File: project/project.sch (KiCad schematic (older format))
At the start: 7 parts

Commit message: fix lib
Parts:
- U?: symbol RockPi:RockPi-S -> project-rescue:RockPi-S-RockPi
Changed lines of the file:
@@
 EESchema Schematic File Version 4
+LIBS:project-cache
 EELAYER 26 0
 EELAYER END
@@
 $EndComp
 $Comp
-L RockPi:RockPi-S U?
+L project-rescue:RockPi-S-RockPi U?
 U 1 1 5FF9F2DF
 P 7750 3550

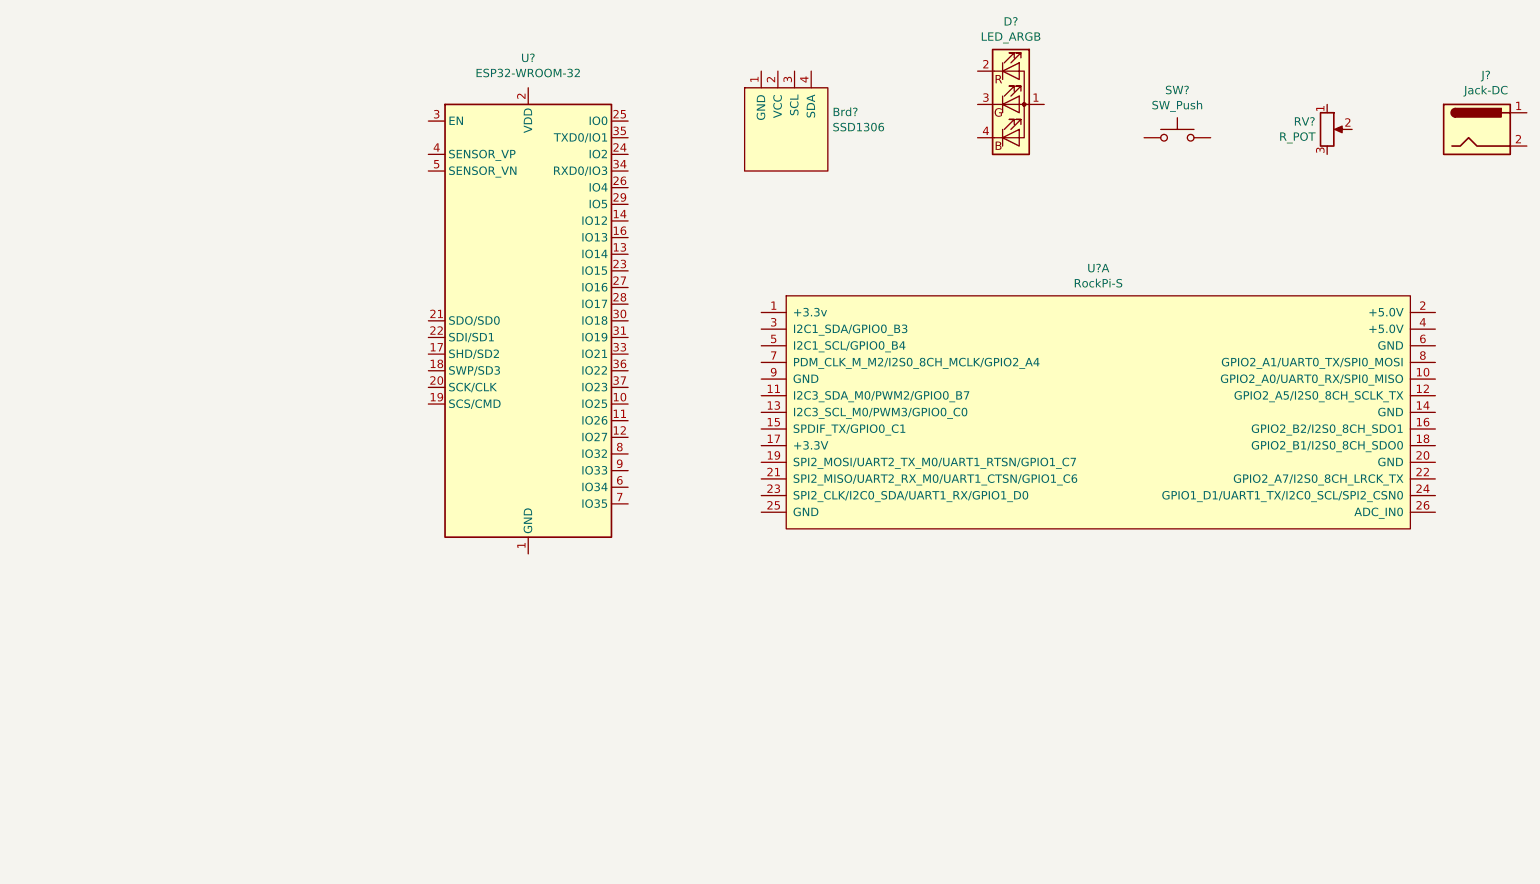
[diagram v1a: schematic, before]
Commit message: add connections, 5V and GND bus
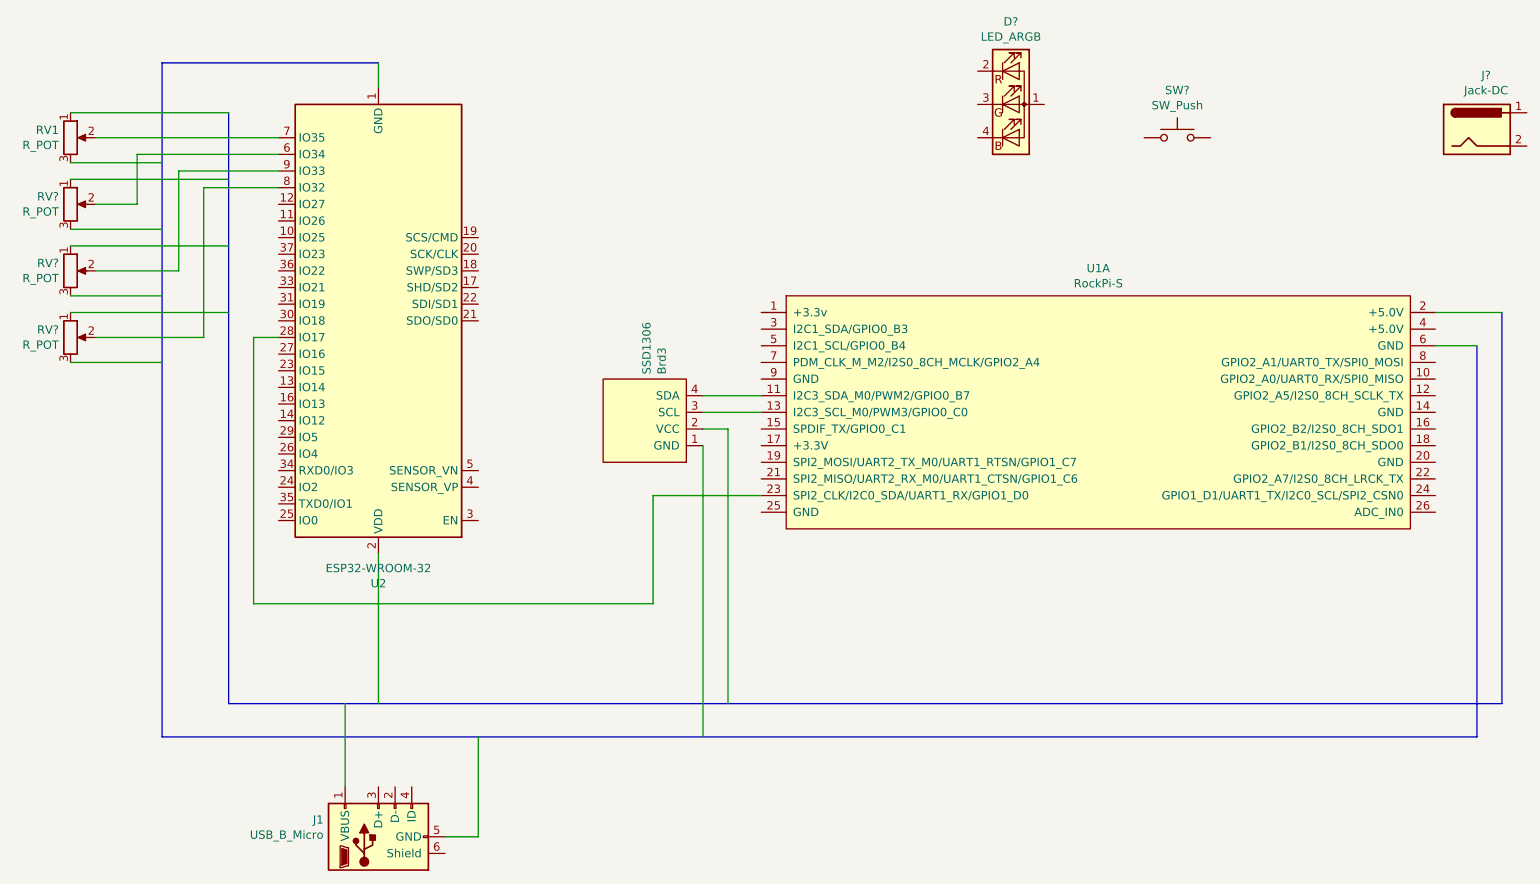
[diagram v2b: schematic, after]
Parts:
- added J1: USB_B_Micro, symbol Connector:USB_B_Micro
- added RV? (x3): R_POT, symbol Device:R_POT
- gave numbers to parts that had none: 4
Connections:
- wire segments 0 -> 35
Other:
- moved on the sheet: Brd3, RV1, U2
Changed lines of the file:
@@
 $EndDescr
 $Comp
-L RF_Module:ESP32-WROOM-32 U?
+L RF_Module:ESP32-WROOM-32 U2
 U 1 1 5FF9F0B8
-P 4200 3000
-F 0 "U?" H 4200 4578 50  0000 C CNN
-F 1 "ESP32-WROOM-32" H 4200 4487 50  0000 C CNN
-F 2 "RF_Module:ESP32-WROOM-32" H 4200 1500 50  0001 C CNN
-F 3 "https://www.espressif.com/sites/default/files/documentation/esp32-wroom-32_datasheet_en.pdf" H 3900 3050 50  0001 C CNN
-	1    4200 3000
-	1    0    0    -1
-$EndComp
-$Comp
-L project-rescue:RockPi-S-RockPi U?
+P 3300 3000
+F 0 "U2" H 3300 4578 50  0000 C CNN
+F 1 "ESP32-WROOM-32" H 3300 4487 50  0000 C CNN
+F 2 "RF_Module:ESP32-WROOM-32" H 3300 1500 50  0001 C CNN
+F 3 "https://www.espressif.com/sites/default/files/documentation/esp32-wroom-32_datasheet_en.pdf" H 3000 3050 50  0001 C CNN
+	1    3300 3000
+	-1   0    0    1
+$EndComp
+$Comp
+L project-rescue:RockPi-S-RockPi U1
 U 1 1 5FF9F2DF
 P 7750 3550
-F 0 "U?" H 7625 4415 50  0000 C CNN
+F 0 "U1" H 7625 4415 50  0000 C CNN
 F 1 "RockPi-S" H 7625 4324 50  0000 C CNN
 F 2 "" H 9600 3600 50  0001 C CNN
@@
 $EndComp
 $Comp
-L SSD1306-128x64_OLED:SSD1306 Brd?
+L SSD1306-128x64_OLED:SSD1306 Brd3
 U 1 1 5FF9F3AC
-P 5750 1850
-F 0 "Brd?" H 6028 1953 50  0000 L CNN
-F 1 "SSD1306" H 6028 1862 50  0000 L CNN
-F 2 "" H 5750 2100 50  0001 C CNN
-F 3 "" H 5750 2100 50  0001 C CNN
-	1    5750 1850
-	1    0    0    -1
+P 4900 3600
+F 0 "Brd3" H 5178 3703 50  0000 L CNN
+F 1 "SSD1306" H 5178 3612 50  0000 L CNN
+F 2 "" H 4900 3850 50  0001 C CNN
+F 3 "" H 4900 3850 50  0001 C CNN
+	1    4900 3600
+	0    1    -1   0
 $EndComp
 $Comp
@@
 $EndComp
 $Comp
-L Device:R_POT RV?
+L Device:R_POT RV1
 U 1 1 5FF9F680
-P 9000 1850
-F 0 "RV?" H 8930 1896 50  0000 R CNN
-F 1 "R_POT" H 8930 1805 50  0000 R CNN
-F 2 "" H 9000 1850 50  0001 C CNN
-F 3 "~" H 9000 1850 50  0001 C CNN
-	1    9000 1850
+P 1450 1900
+F 0 "RV1" H 1380 1946 50  0000 R CNN
+F 1 "R_POT" H 1380 1855 50  0000 R CNN
+F 2 "" H 1450 1900 50  0001 C CNN
+F 3 "~" H 1450 1900 50  0001 C CNN
+	1    1450 1900
 	1    0    0    -1
 $EndComp
@@
 	1    0    0    -1
 $EndComp
+Wire Wire Line
+	5250 3450 5600 3450
+Wire Wire Line
+	5250 3550 5600 3550
+$Comp
+L Connector:USB_B_Micro J1
+U 1 1 5FFA4D52
+P 3300 6100
+F 0 "J1" V 3402 6430 50  0000 L CNN
+F 1 "USB_B_Micro" V 3311 6430 50  0000 L CNN
+F 2 "" H 3450 6050 50  0001 C CNN
+F 3 "~" H 3450 6050 50  0001 C CNN
+	1    3300 6100
+	0    -1   -1   0
+$EndComp
+Wire Wire Line
+	3100 5800 3100 5300
+Wire Wire Line
+	5250 3650 5400 3650
+Wire Wire Line
+	5400 3650 5400 5300
+Wire Wire Line
+	3300 4400 3300 5300
+Wire Bus Line
+	10050 5300 10050 2950
+Wire Wire Line
+	9650 2950 10050 2950
+Wire Bus Line
+	9900 5500 9900 3150
+Wire Wire Line
+	9650 3150 9900 3150
+Wire Wire Line
+	3900 6100 3900 5500
+Wire Wire Line
+	5250 3750 5250 5500
+Wire Bus Line
+	2000 1450 3300 1450
+Wire Wire Line
+	3300 1600 3300 1450
+Wire Wire Line
+	3700 6100 3900 6100
+$Comp
+L Device:R_POT RV?
+U 1 1 5FFA6CA2
+P 1450 2300
+F 0 "RV?" H 1380 2346 50  0000 R CNN
+F 1 "R_POT" H 1380 2255 50  0000 R CNN
+F 2 "" H 1450 2300 50  0001 C CNN
+F 3 "~" H 1450 2300 50  0001 C CNN
+	1    1450 2300
+	1    0    0    -1
+$EndComp
+$Comp
+L Device:R_POT RV?
+U 1 1 5FFA6CE7
+P 1450 2700
+F 0 "RV?" H 1380 2746 50  0000 R CNN
+F 1 "R_POT" H 1380 2655 50  0000 R CNN
+F 2 "" H 1450 2700 50  0001 C CNN
+F 3 "~" H 1450 2700 50  0001 C CNN
+	1    1450 2700
+	1    0    0    -1
+$EndComp
+$Comp
+L Device:R_POT RV?
+U 1 1 5FFA6D19
+P 1450 3100
+F 0 "RV?" H 1380 3146 50  0000 R CNN
+F 1 "R_POT" H 1380 3055 50  0000 R CNN
+F 2 "" H 1450 3100 50  0001 C CNN
+F 3 "~" H 1450 3100 50  0001 C CNN
+	1    1450 3100
+	1    0    0    -1
+$EndComp
+Wire Bus Line
+	2000 1450 2000 5500
+Wire Bus Line
+	2000 5500 9900 5500
+Wire Wire Line
+	5600 4050 4950 4050
+Wire Wire Line
+	4950 4050 4950 4700
+Wire Wire Line
+	4950 4700 2550 4700
+Wire Wire Line
+	2550 4700 2550 3100
+Wire Wire Line
+	2550 3100 2700 3100
+Wire Wire Line
+	1600 1900 2700 1900
+Wire Wire Line
+	1600 2300 1850 2300
+Wire Wire Line
+	1850 2300 1850 2000
+Wire Wire Line
+	1850 2000 2700 2000
+Wire Wire Line
+	2100 2100 2700 2100
+Wire Wire Line
+	1600 2700 2100 2700
+Wire Wire Line
+	2100 2700 2100 2100
+Wire Wire Line
+	1600 3100 2250 3100
+Wire Wire Line
+	2250 3100 2250 2200
+Wire Wire Line
+	2250 2200 2700 2200
+Wire Wire Line
+	1450 2050 2000 2050
+Wire Wire Line
+	1450 2450 2000 2450
+Wire Wire Line
+	1450 2850 2000 2850
+Wire Wire Line
+	1450 3250 2000 3250
+Wire Bus Line
+	2400 5300 2400 1750
+Wire Bus Line
+	2400 5300 10050 5300
+Wire Wire Line
+	1450 1750 2400 1750
+Wire Wire Line
+	1450 2150 2400 2150
+Wire Wire Line
+	1450 2550 2400 2550
+Wire Wire Line
+	1450 2950 2400 2950
 $EndSCHEMATC
